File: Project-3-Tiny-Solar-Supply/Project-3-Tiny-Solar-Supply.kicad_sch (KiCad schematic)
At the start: 0 parts

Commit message: add components and new symbols and footprints libraries
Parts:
- added C1, C2, C3: C, symbol Device:C
- added D1, D2: SS14, Diode_SMD:D_SMA, symbol Diode:SS14
- added J1, J2, J3, J4: Conn_01x02_Pin, symbol Connector:Conn_01x02_Pin
- added L1: ASPI-0630LR-100M-T15, ASPI-0630LR-100M-T15:IND_ASPI-0630LR-100M-T15, symbol ASPI-0630LR-100M-T15:ASPI-0630LR-100M-T15
- added Q1: 2N7002, Package_TO_SOT_SMD:SOT-23, symbol Transistor_FET:2N7002
- added R1, R2, R3, R4: R, symbol Device:R
- added U1: AP3015AKTR-G1, AP3015AKTR-G1:SOT95P280X145-5N, symbol AP3015AKTR-G1:AP3015AKTR-G1

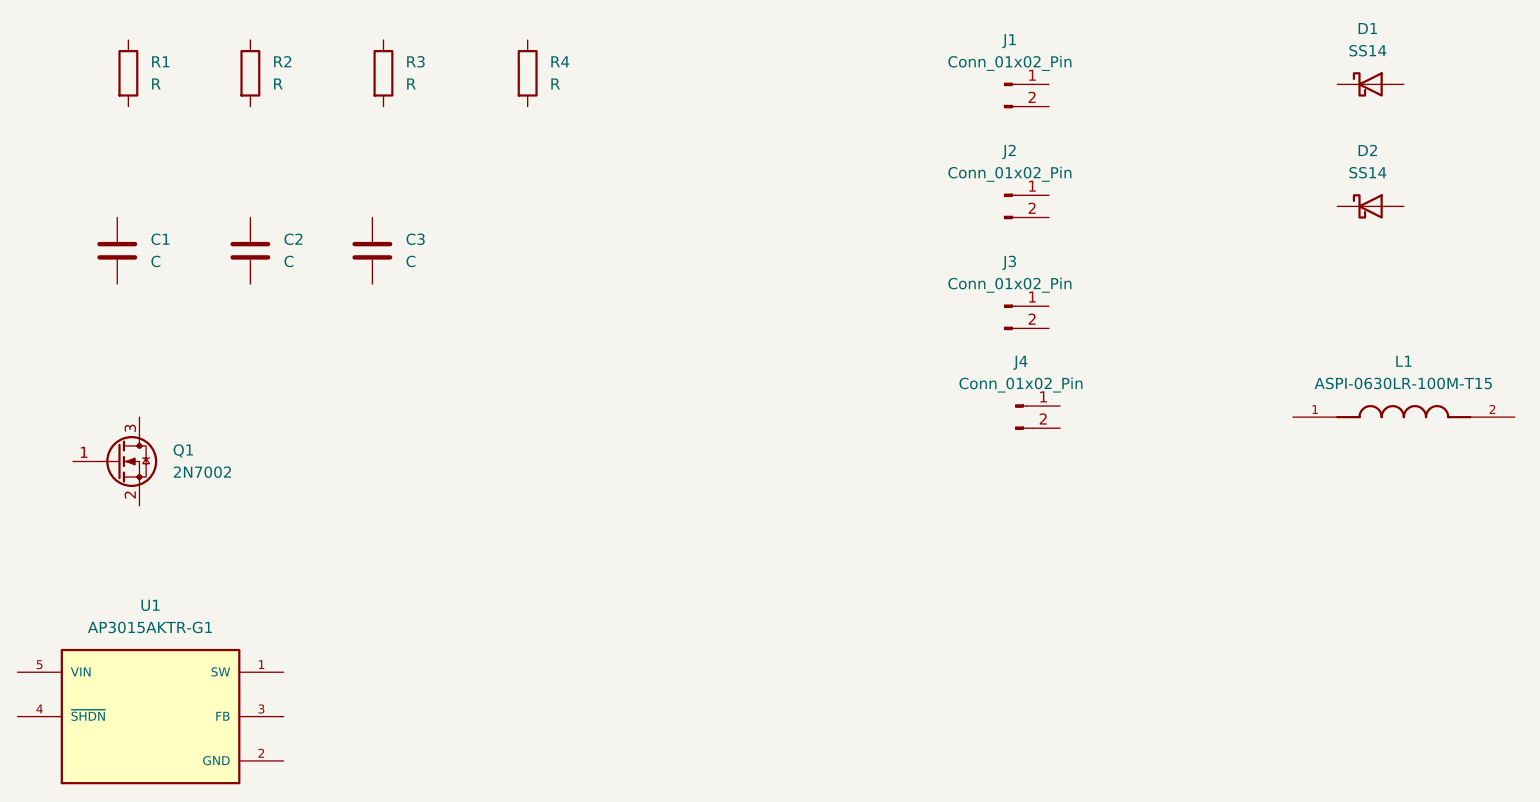
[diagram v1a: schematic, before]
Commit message: add symbols' values and link some footprints
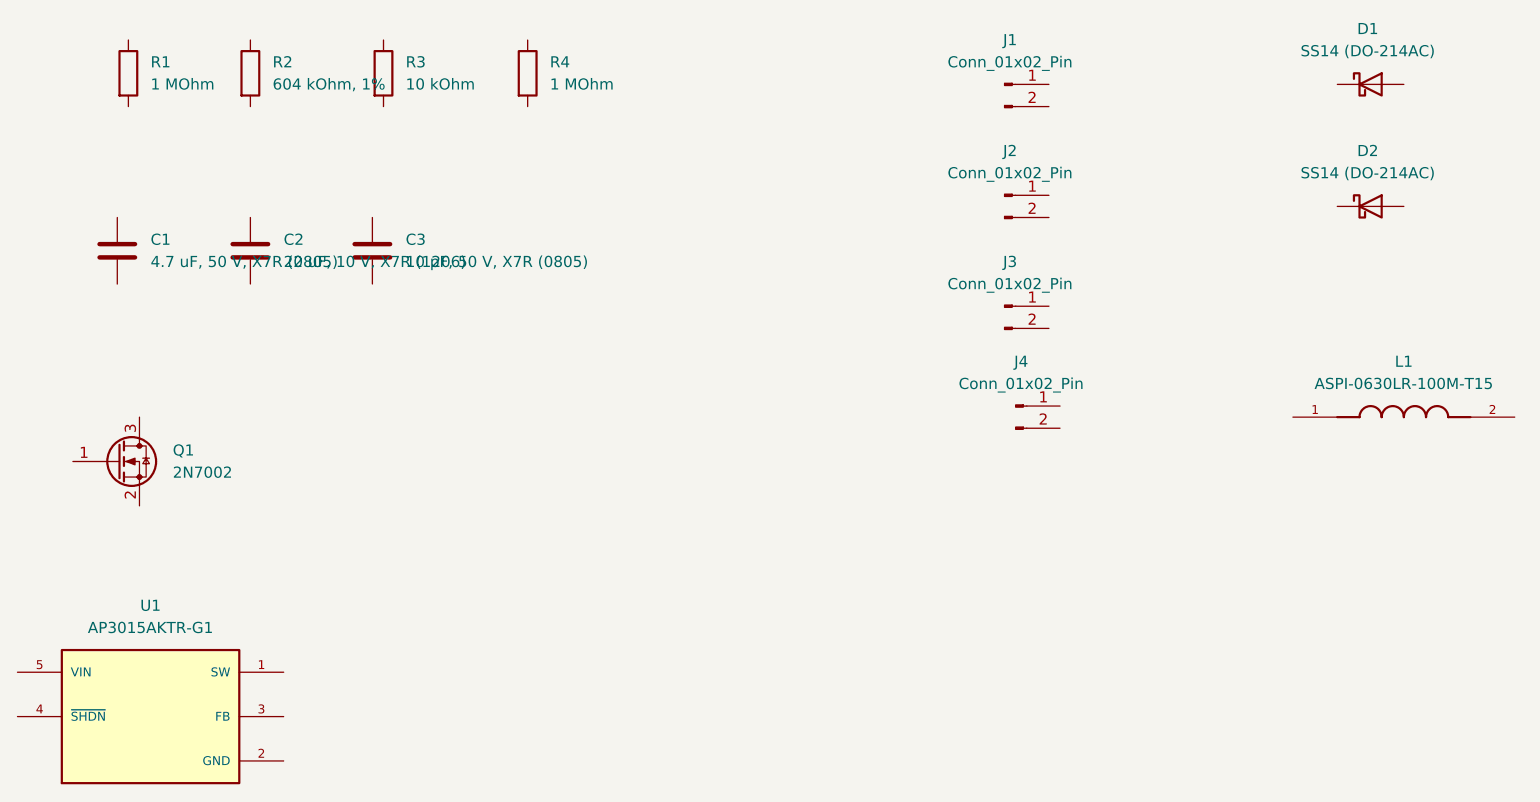
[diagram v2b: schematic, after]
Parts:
- C1: value C -> 4.7 uF, 50 V, X7R (0805)
- C2: value C -> 22 uF, 10 V, X7R (1206)
- C3: value C -> 10 pF, 50 V, X7R (0805)
- D1, D2: value SS14 -> SS14 (DO-214AC); footprint Diode_SMD:D_SMA -> SS14:DO-214AC
- R1, R4: value R -> 1 MOhm
- R2: value R -> 604 kOhm, 1%
- R3: value R -> 10 kOhm
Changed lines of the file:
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@@
 			)
 		)
-		(property "Value" "R"
+		(property "Value" "10 kOhm"
 			(at 86.36 52.0699 0)
 			(show_name no)
@@
 			)
 		)
-		(property "Value" "C"
+		(property "Value" "10 pF, 50 V, X7R (0805)"
 			(at 86.36 72.3899 0)
 			(show_name no)
@@
 			)
 		)
-		(property "Value" "SS14"
+		(property "Value" "SS14 (DO-214AC)"
 			(at 196.5325 48.26 0)
 			(show_name no)
@@
 			)
 		)
-		(property "Footprint" "Diode_SMD:D_SMA"
+		(property "Footprint" "SS14:DO-214AC"
 			(at 196.85 56.515 0)
 			(hide yes)
@@
 			)
 		)
-		(property "Value" "R"
+		(property "Value" "1 MOhm"
 			(at 102.87 52.0699 0)
 			(show_name no)
@@
 			)
 		)
-		(property "Value" "R"
+		(property "Value" "604 kOhm, 1%"
 			(at 71.12 52.0699 0)
 			(show_name no)
@@
 			)
 		)
-		(property "Value" "SS14"
+		(property "Value" "SS14 (DO-214AC)"
 			(at 196.5325 62.23 0)
 			(show_name no)
@@
 			)
 		)
-		(property "Footprint" "Diode_SMD:D_SMA"
+		(property "Footprint" "SS14:DO-214AC"
 			(at 196.85 70.485 0)
 			(hide yes)
@@
 			)
 		)
-		(property "Value" "C"
+		(property "Value" "22 uF, 10 V, X7R (1206)"
 			(at 72.39 72.3899 0)
 			(show_name no)
@@
 			)
 		)
-		(property "Value" "R"
+		(property "Value" "1 MOhm"
 			(at 57.15 52.0699 0)
 			(show_name no)
@@
 			)
 		)
-		(property "Value" "C"
+		(property "Value" "4.7 uF, 50 V, X7R (0805)"
 			(at 57.15 72.3899 0)
 			(show_name no)
